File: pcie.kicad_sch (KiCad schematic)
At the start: 30 parts, among them J8 1-2199230-6, U1 MIMX8MM6DVTLZAA, U34 SI52112-B5-GM2, U35 74LVC1G07, U36 74LVC1G07, Y4 25MHz

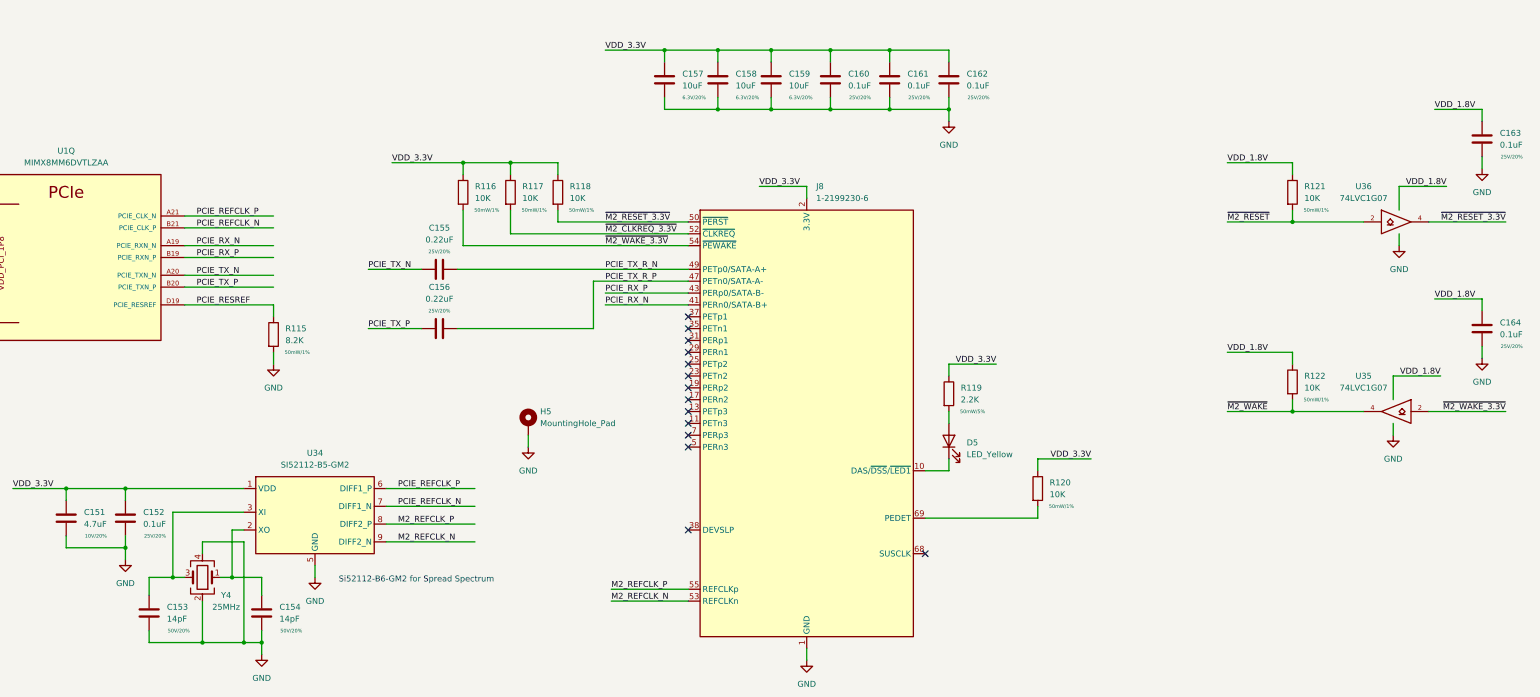
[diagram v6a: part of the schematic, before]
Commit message: v2 of ddr flytimes tool, lots of routing work, sch fixes
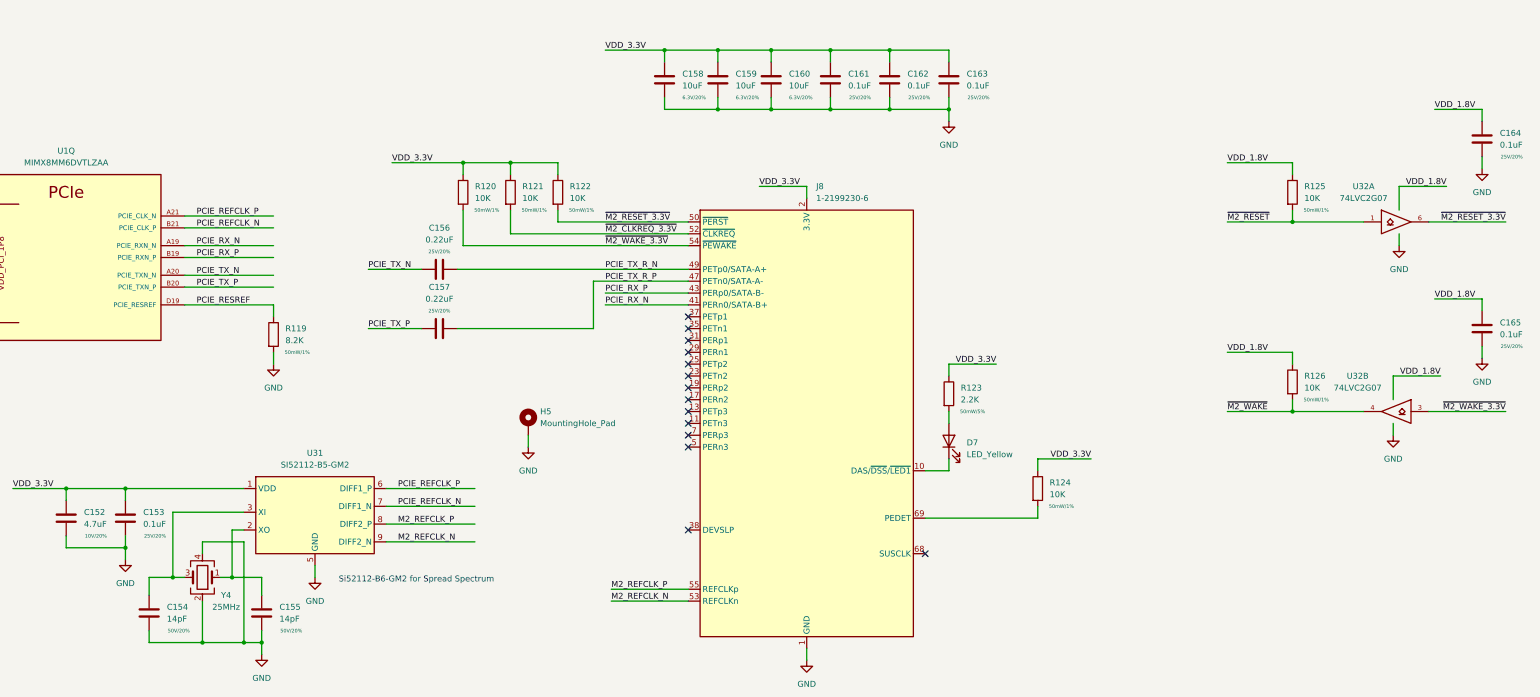
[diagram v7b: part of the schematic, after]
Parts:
- removed U35, U36: 74LVC1G07, Package_TO_SOT_SMD:SOT-23-5, symbol 74xGxx:74LVC1G07
- added U32: 74LVC2G07, Package_TO_SOT_SMD:SOT-886, symbol 74xGxx:74LVC2G07
- C156: renamed from C155; footprint Capacitor_SMD:C_0402_1005Metric -> qsbc:C_0201_0603Metric
- C157: renamed from C156; footprint Capacitor_SMD:C_0402_1005Metric -> qsbc:C_0201_0603Metric
- renumbered C151 to C152, C152 to C153, C153 to C154, C154 to C155, C157 to C158, C158 to C159, C159 to C160, C160 to C161, C161 to C162, C162 to C163, C163 to C164, C164 to C165, D5 to D7, R115 to R119, R116 to R120, R117 to R121, R118 to R122, R119 to R123, R120 to R124, R121 to R125, R122 to R126, U34 to U31
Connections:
- net GND: now also U32.2 (GND), U32.2 (GND)
- net VCC: now also U32.5 (VCC), U32.5 (VCC)
- net ~{M2_RESET_3.3V}: now also U32.6
- net ~{M2_RESET}: now also U32.1
- net ~{M2_WAKE_3.3V}: now also U32.3
- net ~{M2_WAKE}: now also U32.4

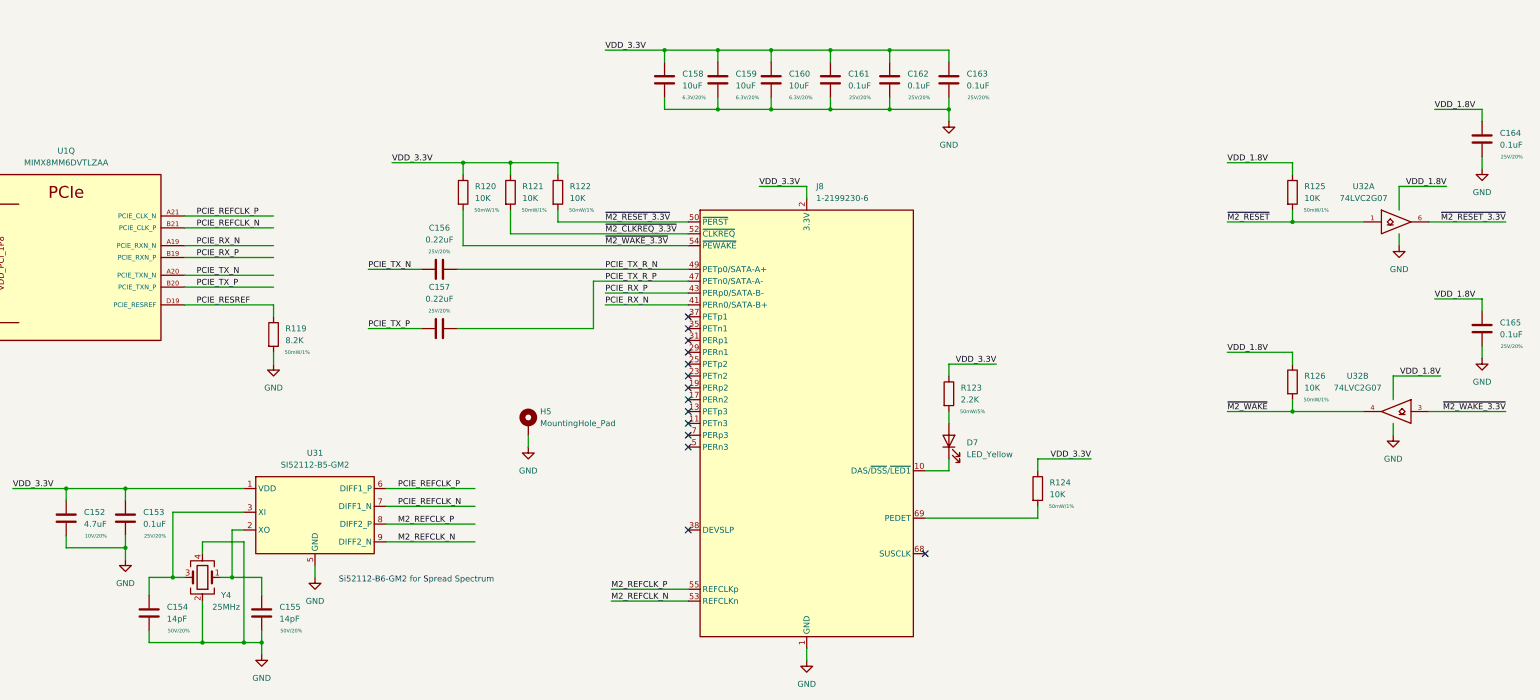
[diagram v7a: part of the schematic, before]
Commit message: more routing work, prepare to change to x32 lpddr4
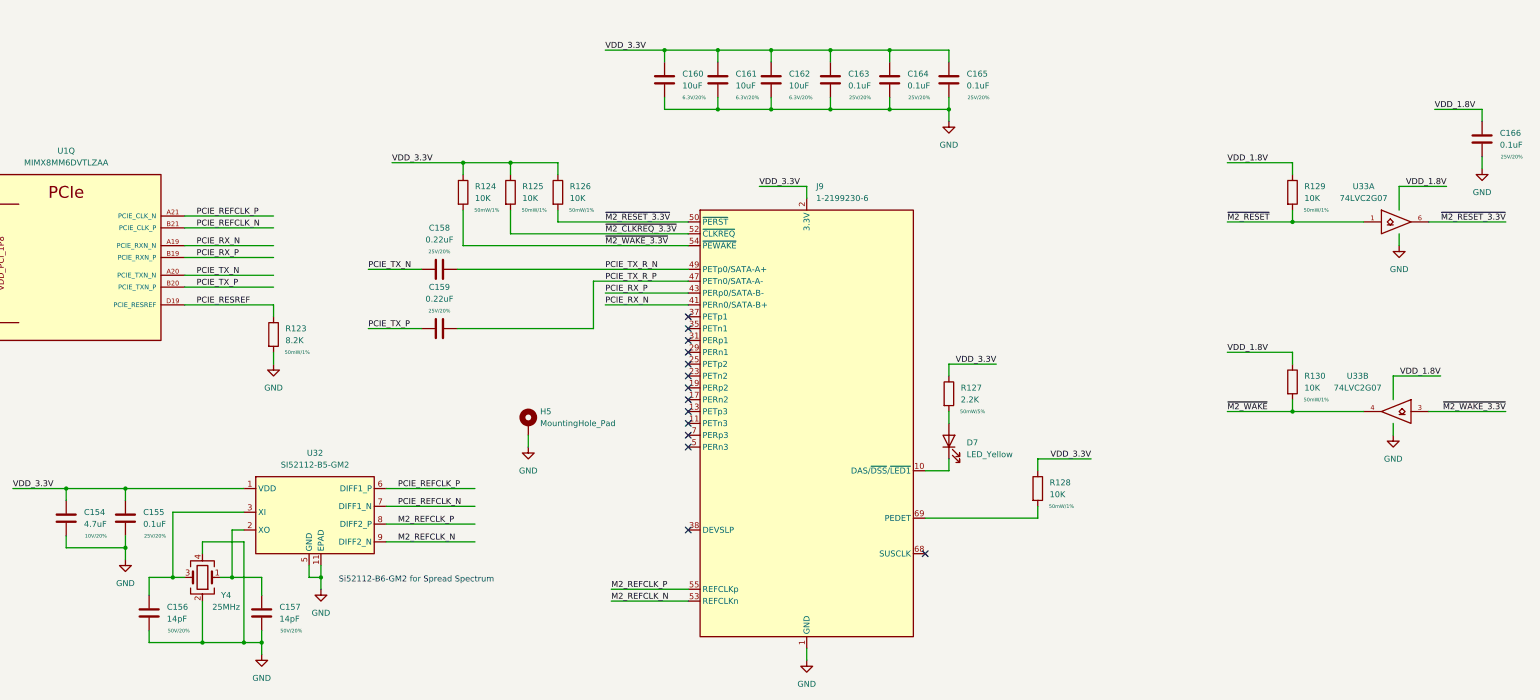
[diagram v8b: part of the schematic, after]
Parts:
- removed C165: 0.1uF, Capacitor_SMD:C_0402_1005Metric, symbol Device:C
- renumbered C152 to C154, C153 to C155, C154 to C156, C155 to C157, C156 to C158, C157 to C159, C158 to C160, C159 to C161, C160 to C162, C161 to C163, C162 to C164, C163 to C165, C164 to C166, J8 to J9, R119 to R123, R120 to R124, R121 to R125, R122 to R126, R123 to R127, R124 to R128, R125 to R129, R126 to R130, U31 to U32, U32 to U33
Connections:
- net GND: now also U32.11 (EPAD)
